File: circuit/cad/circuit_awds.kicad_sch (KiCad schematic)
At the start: 5 parts, among them K1 SILxx-1Axx-71x, K2 SILxx-1Axx-71x, K3 SILxx-1Axx-71x, K4 SILxx-1Axx-71x, U1 ESP32-WROOM-32

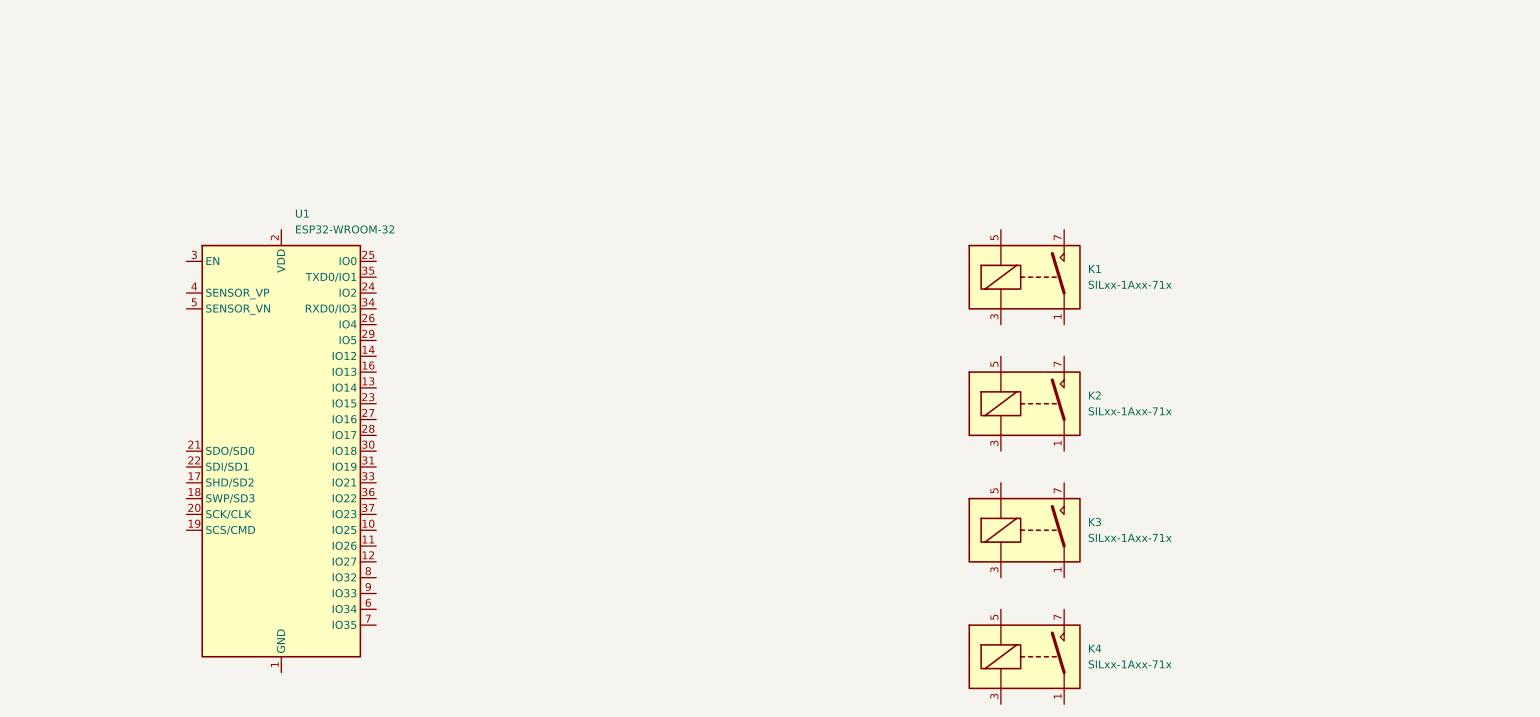
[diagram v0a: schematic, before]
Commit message: Added Command and Switch Modules
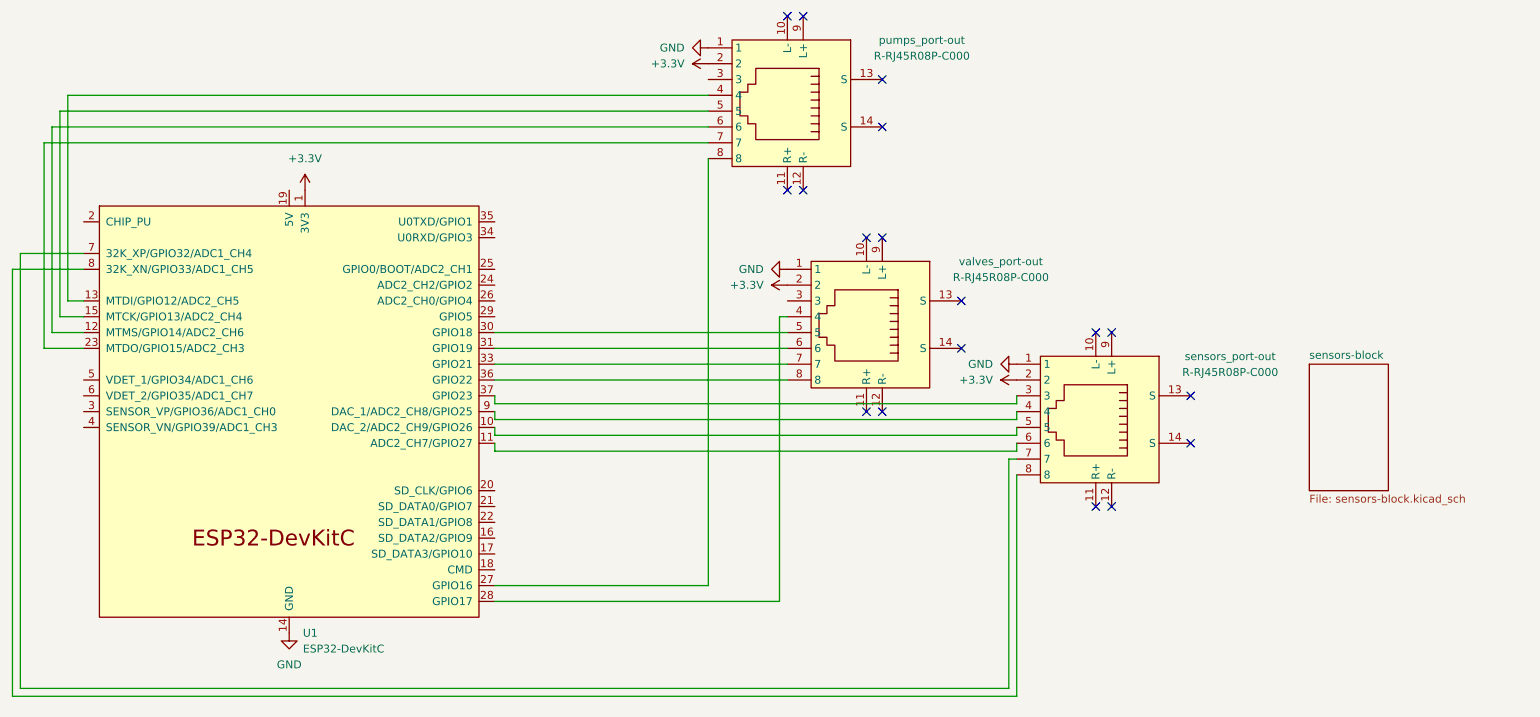
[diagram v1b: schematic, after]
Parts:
- removed K1, K2, K3, K4: SILxx-1Axx-71x, Relay_THT:Relay_SPST_StandexMeder_SIL_Form1A, symbol Relay:SILxx-1Axx-71x
- removed U1: ESP32-WROOM-32, RF_Module:ESP32-WROOM-32, symbol RF_Module:ESP32-WROOM-32
- added U1: ESP32-DevKitC, PCM_Espressif:ESP32-DevKitC, symbol PCM_Espressif:ESP32-DevKitC
- added pumps_port-out, sensors_port-out, valves_port-out: R-RJ45R08P-C000, easyeda2kicad:RJ45-TH_R-RJ45R08P-C000, symbol easyeda2kicad:R-RJ45R08P-C000
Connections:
- new net: U1.28 (GPIO17), valves_port-out.4
- new net: U1.30 (GPIO18), valves_port-out.5
- new net: U1.31 (GPIO19), valves_port-out.6
- new net: U1.33 (GPIO21), valves_port-out.7
- new net: U1.36 (GPIO22), valves_port-out.8
- new net: U1.10 (DAC_2/ADC2_CH9/GPIO26), sensors_port-out.5
- new net: U1.11 (ADC2_CH7/GPIO27), sensors_port-out.6
- new net: U1.12 (MTMS/GPIO14/ADC2_CH6), pumps_port-out.6
- new net: U1.13 (MTDI/GPIO12/ADC2_CH5), pumps_port-out.4
- new net: U1.15 (MTCK/GPIO13/ADC2_CH4), pumps_port-out.5
- new net: U1.23 (MTDO/GPIO15/ADC2_CH3), pumps_port-out.7
- new net: U1.27 (GPIO16), pumps_port-out.8
- new net: U1.37 (GPIO23), sensors_port-out.3
- new net: U1.7 (32K_XP/GPIO32/ADC1_CH4), sensors_port-out.7
- new net: U1.8 (32K_XN/GPIO33/ADC1_CH5), sensors_port-out.8
- new net: U1.9 (DAC_1/ADC2_CH8/GPIO25), sensors_port-out.4
- new net +3.3V: U1.1 (3V3), pumps_port-out.2, sensors_port-out.2, valves_port-out.2
- new net GND: U1.14 (GND), U1.32 (GND), U1.38 (GND), pumps_port-out.1, sensors_port-out.1, valves_port-out.1
- no-connect marks 0 -> 18
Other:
- added sheet sensors-block (sensors-block.kicad_sch)
